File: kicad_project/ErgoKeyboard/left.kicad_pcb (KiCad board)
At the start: 2 copper layers, 171.9 x 107.2 mm, 58 parts

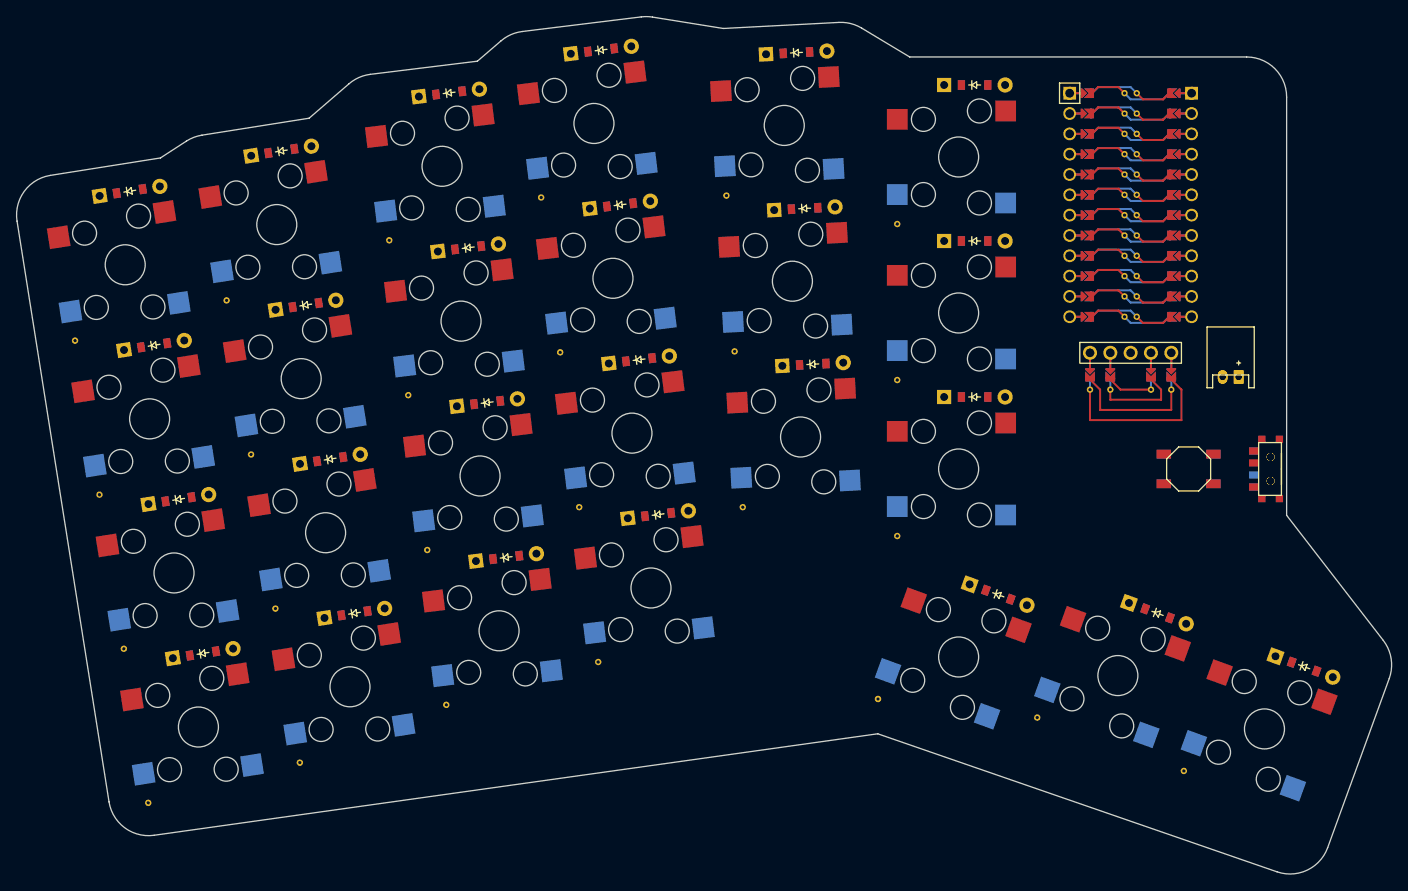
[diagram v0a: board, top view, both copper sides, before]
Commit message: fixed oled, started routing
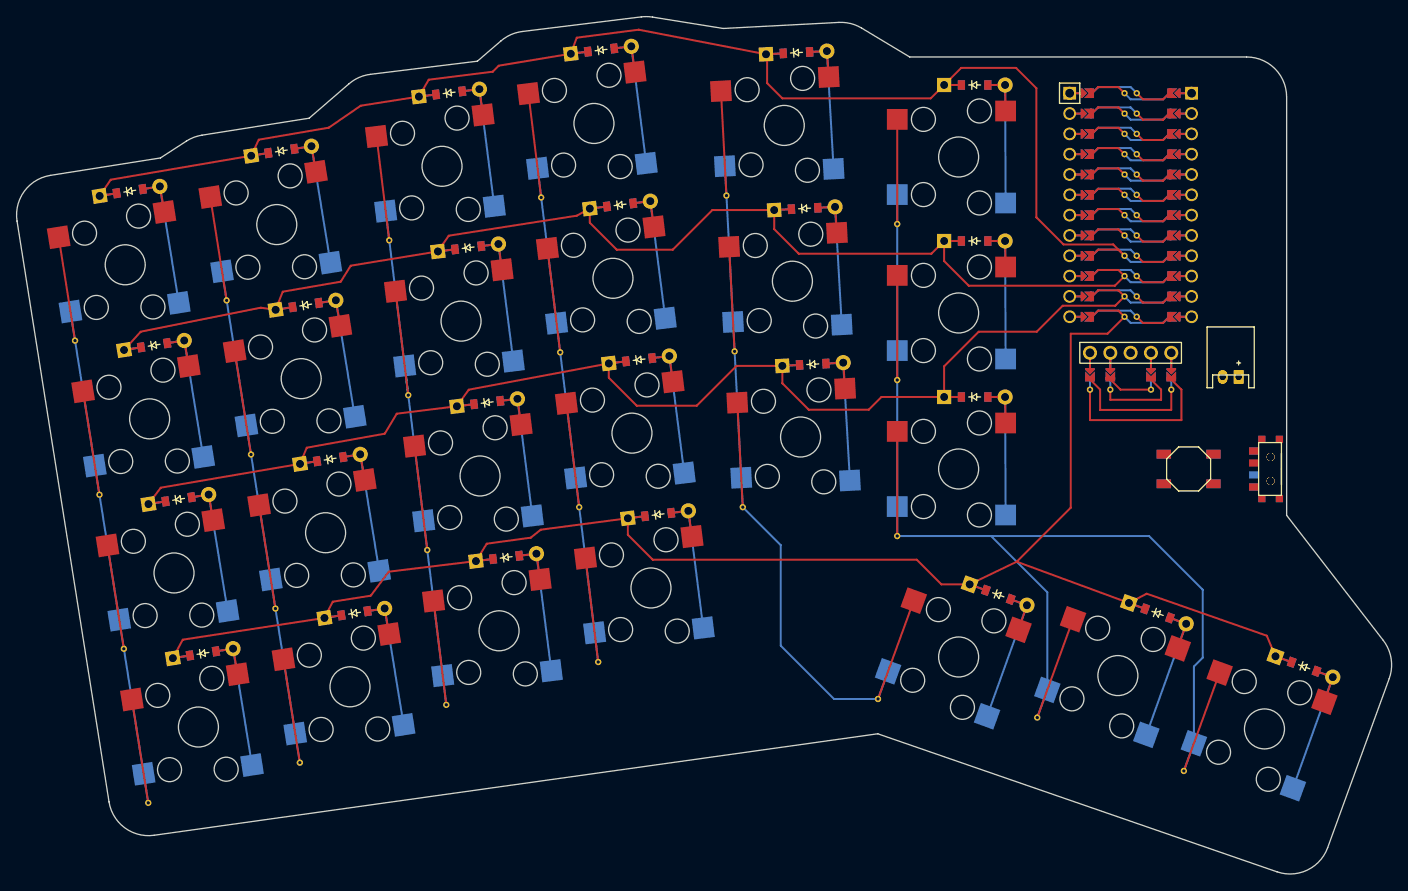
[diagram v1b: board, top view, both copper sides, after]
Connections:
- OLED1 pad : P2 -> P1
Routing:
- net P9: track 0.00 -> 222.4 mm
- net P19: track 0.00 -> 210.0 mm
- net P6: track 0.00 -> 186.5 mm
- net P8: track 0.00 -> 170.5 mm
- net P7: track 0.00 -> 170.5 mm
- net P18: track 0.00 -> 132.9 mm
- net P14: track 0.00 -> 118.2 mm
- net P15: track 0.00 -> 114.5 mm
- net P10: track 0.00 -> 114.5 mm
- net P16: track 0.00 -> 114.5 mm
- net index_home: track 0.00 -> 22.3 mm
- net index_top: track 0.00 -> 22.3 mm
- net index_bottom: track 0.00 -> 22.3 mm
- net inner_bottom: track 0.00 -> 22.3 mm
- net inner_top: track 0.00 -> 22.3 mm
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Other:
- net class Default removed

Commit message: trying some stuff out
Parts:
- moved D10 7.62 mm to (213.6, 117.0), turned to -83 degrees
- moved D18 7.62 mm to (253.1, 93.2), turned to -87 degrees
- moved D19 7.62 mm to (252.1, 73.8), turned to -87 degrees
- moved D3 7.62 mm to (172.1, 109.6), turned to -81 degrees
- moved D6 7.62 mm to (194.1, 123.8), turned to -81 degrees
- moved D1 7.62 mm to (178.2, 148.1), turned to -81 degrees
- moved D2 7.62 mm to (175.1, 128.8), turned to -81 degrees
- moved D4 7.62 mm to (169.0, 90.3), turned to -81 degrees
- moved D7 7.62 mm to (191.0, 104.5), turned to -81 degrees
- moved D5 7.62 mm to (197.1, 143.1), turned to -81 degrees
- moved D24 7.62 mm to (295.7, 146.4), turned to -110 degrees
- moved D25 7.62 mm to (314.0, 153.1), turned to -110 degrees
- moved D8 7.62 mm to (188.0, 85.3), turned to -81 degrees
- moved D20 7.62 mm to (274.2, 117.2), turned to -90 degrees
- moved D21 7.62 mm to (274.2, 97.7), turned to -90 degrees
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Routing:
- net P9: track 222.4 -> 131.0 mm
- net P19: track 210.0 -> 135.0 mm
- net P6: track 186.5 -> 136.2 mm
- net P8: track 170.5 -> 130.8 mm
- net P7: track 170.5 -> 134.8 mm
- net P18: track 132.9 -> 98.7 mm
- net outer_mod: track 22.3 -> 16.3 mm
- net outer_top: track 22.3 -> 16.3 mm
- net outer_home: track 22.3 -> 16.3 mm
- net outer_bottom: track 22.3 -> 16.3 mm
- net pinky_mod: track 22.3 -> 16.3 mm
- net index_home: track 22.3 -> 16.3 mm
- net index_top: track 22.3 -> 16.3 mm
- net index_bottom: track 22.3 -> 16.3 mm
- net ring_home: track 22.3 -> 16.3 mm
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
